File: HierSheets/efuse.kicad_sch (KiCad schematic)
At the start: 1 part, among them U15 TPS25983

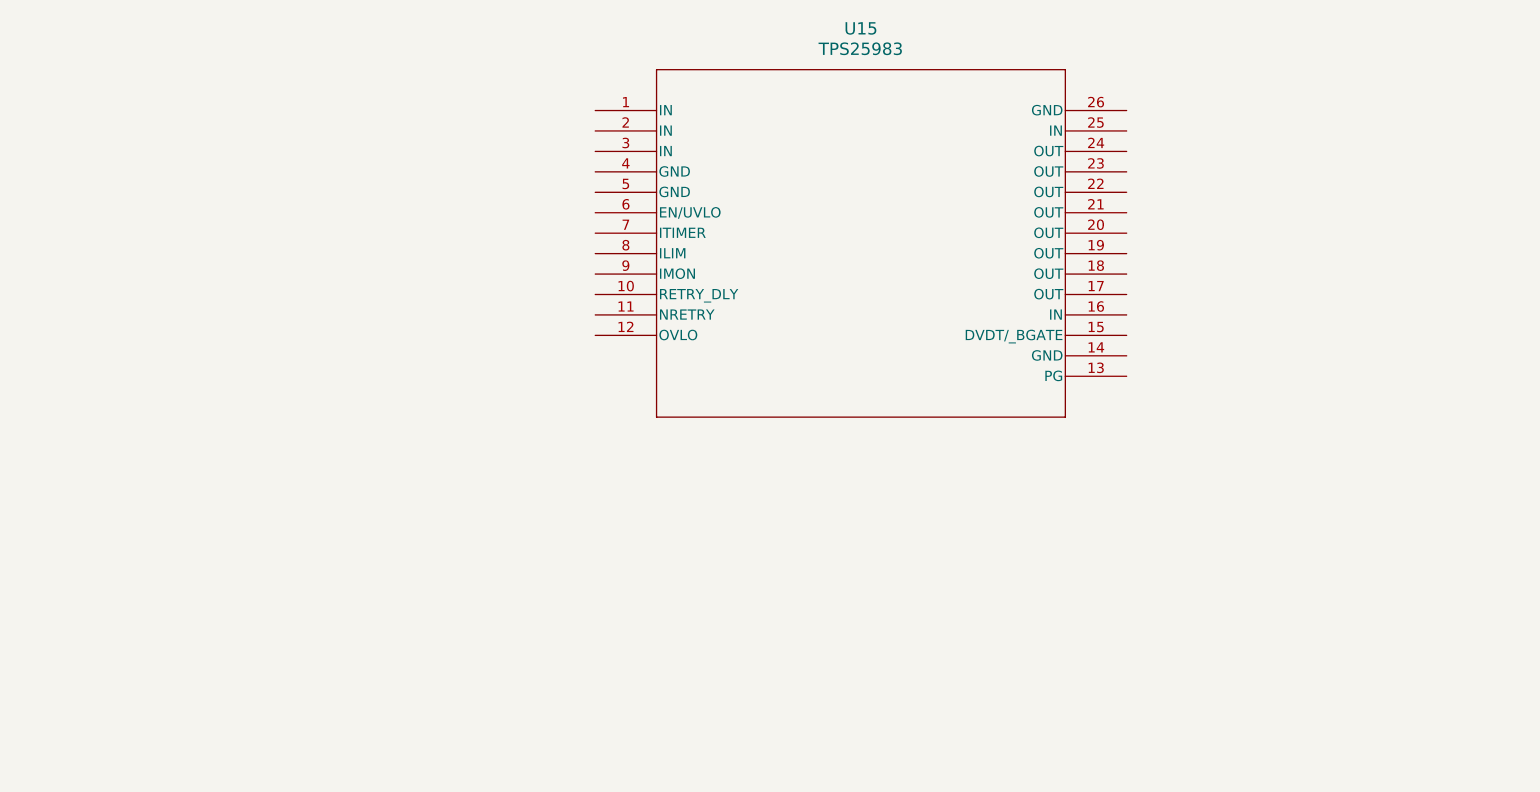
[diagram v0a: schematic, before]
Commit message: Efuse added, not set.
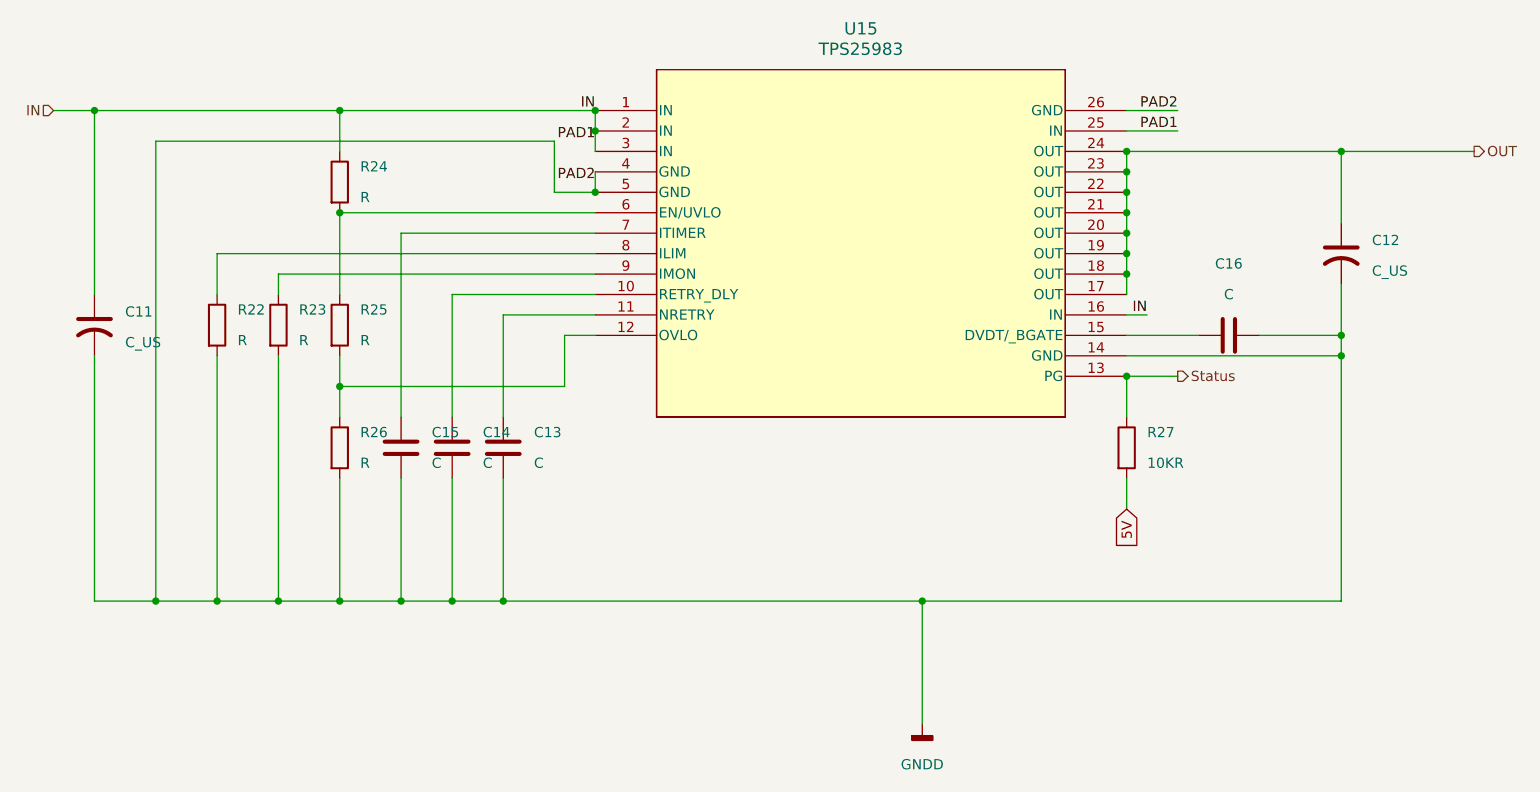
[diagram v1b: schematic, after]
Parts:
- added C11, C12: C_US, symbol Device:C_US
- added C13, C14, C15, C16: C, symbol Device:C
- added R22, R23, R24, R25, R26: R, symbol Device:R
- added R27: 10KR, symbol Device:R
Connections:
- net IN: now reaches U15.1 (IN)
- net IN: now also U15.16 (IN), U15.2 (IN), U15.25 (IN), U15.3 (IN), C11.1, R24.1
- net at U15.10 (RETRY_DLY): now also C14.1
- net at U15.11 (NRETRY): now also C13.1
- net at U15.12 (OVLO): now also R25.2, R26.1
- net Status: now reaches U15.13 (PG)
- net Status: now also R27.1
- net GNDD: now reaches U15.14 (GND)
- net GNDD: now also U15.26 (GND), U15.4 (GND), U15.5 (GND), C11.2, C12.2, C13.2, C14.2, C15.2, C16.1, R22.2, R23.2, R26.2
- net at U15.15 (DVDT/_BGATE): now also C16.2
- net OUT: now reaches U15.17 (OUT)
- net OUT: now also U15.18 (OUT), U15.19 (OUT), U15.20 (OUT), U15.21 (OUT), U15.22 (OUT), U15.23 (OUT), U15.24 (OUT), C12.1
- net at U15.6 (EN/UVLO): now also R24.2, R25.1
- net at U15.7 (ITIMER): now also C15.1
- net at U15.8 (ILIM): now also R22.1
- net at U15.9 (IMON): now also R23.1
- new net 5V: R27.2

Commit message: Added kicker, interrupt, I2C pullups, buck converter, button
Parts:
- renumbered C11 to C16, C15 to C17, C14 to C18, C13 to C19, C16 to C20, C12 to C21, R22 to R47, R23 to R48, R24 to R49, R25 to R50, R26 to R51, R27 to R52, U15 to U17
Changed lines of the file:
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@@
 		(dnp no)
 		(fields_autoplaced yes)
-		(property "Reference" "R24"
+		(property "Reference" "R49"
 			(at 77.47 75.5649 0)
 			(show_name no)
@@
 			(project "Prototyp_0.1"
 				(path "/607d4431-9cfb-431e-bb0d-e8da578e6786/13f8df48-936f-4e77-b00c-1cf58e669057"
-					(reference "R24")
+					(reference "R49")
 					(unit 1)
 				)
@@
 		(dnp no)
 		(fields_autoplaced yes)
-		(property "Reference" "#PWR044"
+		(property "Reference" "#PWR055"
 			(at 147.32 151.13 0)
 			(hide yes)
@@
 			(project "Prototyp_0.1"
 				(path "/607d4431-9cfb-431e-bb0d-e8da578e6786/13f8df48-936f-4e77-b00c-1cf58e669057"
-					(reference "#PWR044")
+					(reference "#PWR055")
 					(unit 1)
 				)
@@
 		(dnp no)
 		(fields_autoplaced yes)
-		(property "Reference" "C11"
+		(property "Reference" "C16"
 			(at 48.26 93.5989 0)
 			(show_name no)
@@
 			(project "Prototyp_0.1"
 				(path "/607d4431-9cfb-431e-bb0d-e8da578e6786/13f8df48-936f-4e77-b00c-1cf58e669057"
-					(reference "C11")
+					(reference "C16")
 					(unit 1)
 				)
@@
 		(dnp no)
 		(fields_autoplaced yes)
-		(property "Reference" "C14"
+		(property "Reference" "C18"
 			(at 92.71 108.5849 0)
 			(show_name no)
@@
 			(project "Prototyp_0.1"
 				(path "/607d4431-9cfb-431e-bb0d-e8da578e6786/13f8df48-936f-4e77-b00c-1cf58e669057"
-					(reference "C14")
+					(reference "C18")
 					(unit 1)
 				)
@@
 		(dnp no)
 		(fields_autoplaced yes)
-		(property "Reference" "R27"
+		(property "Reference" "R52"
 			(at 175.26 108.5849 0)
 			(show_name no)
@@
 			(project "Prototyp_0.1"
 				(path "/607d4431-9cfb-431e-bb0d-e8da578e6786/13f8df48-936f-4e77-b00c-1cf58e669057"
-					(reference "R27")
+					(reference "R52")
 					(unit 1)
 				)
@@
 		(dnp no)
 		(fields_autoplaced yes)
-		(property "Reference" "C16"
+		(property "Reference" "C20"
 			(at 185.42 87.63 90)
 			(show_name no)
@@
 			(project "Prototyp_0.1"
 				(path "/607d4431-9cfb-431e-bb0d-e8da578e6786/13f8df48-936f-4e77-b00c-1cf58e669057"
-					(reference "C16")
+					(reference "C20")
 					(unit 1)
 				)
@@
 		(dnp no)
 		(fields_autoplaced yes)
-		(property "Reference" "C12"
+		(property "Reference" "C21"
 			(at 203.2 84.7089 0)
 			(show_name no)
@@
 			(project "Prototyp_0.1"
 				(path "/607d4431-9cfb-431e-bb0d-e8da578e6786/13f8df48-936f-4e77-b00c-1cf58e669057"
-					(reference "C12")
+					(reference "C21")
 					(unit 1)
 				)
@@
 		(dnp no)
 		(fields_autoplaced yes)
-		(property "Reference" "C15"
+		(property "Reference" "C17"
 			(at 86.36 108.5849 0)
 			(show_name no)
@@
 			(project "Prototyp_0.1"
 				(path "/607d4431-9cfb-431e-bb0d-e8da578e6786/13f8df48-936f-4e77-b00c-1cf58e669057"
-					(reference "C15")
+					(reference "C17")
 					(unit 1)
 				)
@@
 		(dnp no)
 		(fields_autoplaced yes)
-		(property "Reference" "R23"
+		(property "Reference" "R48"
 			(at 69.85 93.3449 0)
 			(show_name no)
@@
 			(project "Prototyp_0.1"
 				(path "/607d4431-9cfb-431e-bb0d-e8da578e6786/13f8df48-936f-4e77-b00c-1cf58e669057"
-					(reference "R23")
+					(reference "R48")
 					(unit 1)
 				)
@@
 		(dnp no)
 		(fields_autoplaced yes)
-		(property "Reference" "R26"
+		(property "Reference" "R51"
 			(at 77.47 108.5849 0)
 			(show_name no)
@@
 			(project "Prototyp_0.1"
 				(path "/607d4431-9cfb-431e-bb0d-e8da578e6786/13f8df48-936f-4e77-b00c-1cf58e669057"
-					(reference "R26")
+					(reference "R51")
 					(unit 1)
 				)
@@
 		(dnp no)
 		(fields_autoplaced yes)
-		(property "Reference" "U15"
+		(property "Reference" "U17"
 			(at 139.7 58.42 0)
 			(show_name no)
@@
 			(project "Prototyp_0.1"
 				(path "/607d4431-9cfb-431e-bb0d-e8da578e6786/13f8df48-936f-4e77-b00c-1cf58e669057"
-					(reference "U15")
+					(reference "U17")
 					(unit 1)
 				)
@@
 		(dnp no)
 		(fields_autoplaced yes)
-		(property "Reference" "C13"
+		(property "Reference" "C19"
 			(at 99.06 108.5849 0)
 			(show_name no)
@@
 			(project "Prototyp_0.1"
 				(path "/607d4431-9cfb-431e-bb0d-e8da578e6786/13f8df48-936f-4e77-b00c-1cf58e669057"
-					(reference "C13")
+					(reference "C19")
 					(unit 1)
 				)
@@
 		(dnp no)
 		(fields_autoplaced yes)
-		(property "Reference" "R25"
+		(property "Reference" "R50"
 			(at 77.47 93.3449 0)
 			(show_name no)
@@
 			(project "Prototyp_0.1"
 				(path "/607d4431-9cfb-431e-bb0d-e8da578e6786/13f8df48-936f-4e77-b00c-1cf58e669057"
-					(reference "R25")
+					(reference "R50")
 					(unit 1)
 				)
@@
 		(dnp no)
 		(fields_autoplaced yes)
-		(property "Reference" "R22"
+		(property "Reference" "R47"
 			(at 62.23 93.3449 0)
 			(show_name no)
@@
 			(project "Prototyp_0.1"
 				(path "/607d4431-9cfb-431e-bb0d-e8da578e6786/13f8df48-936f-4e77-b00c-1cf58e669057"
-					(reference "R22")
-					(unit 1)
-				)
+					(reference "R47")
+					(unit 1)
+				)
